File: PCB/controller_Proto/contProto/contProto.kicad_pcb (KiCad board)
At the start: 2 copper layers, 40 parts, among them J1 Conn_01x05, J10 JST_1mm_3, J11 JST_1mm_3, J12 Conn_01x04, J15 Conn_01x04, J16 Conn_01x04, J2 Conn_01x04, J3 Conn_01x05, J4 Conn_01x04, J5 Conn_01x05, J6 Conn_01x05, J7 Conn_01x05, J8 Conn_01x05, J9 Conn_01x04, SW1 SMD_12x12mm_h8.5mm, SW10 SMD_12x12mm_h8.5mm, SW11 SMD_12x12mm_h8.5mm, SW12 SMD_12x12mm_h8.5mm, SW13 SMD_12x12mm_h8.5mm, SW14 SMD_12x12mm_h8.5mm, SW15 SMD_12x12mm_h8.5mm, SW16 SMD_12x12mm_h8.5mm, SW2 SMD_12x12mm_h8.5mm, SW3 SMD_12x12mm_h8.5mm, SW4 SMD_12x12mm_h8.5mm, SW5 SMD_12x12mm_h8.5mm, SW6 SMD_12x12mm_h8.5mm, SW7 SMD_12x12mm_h8.5mm, SW8 SMD_12x12mm_h8.5mm, SW9 SMD_12x12mm_h8.5mm, U1 ProMicroC, U2 ProMicroC, U3 DRV5033FAxLPG, U4 DRV5033FAxLPG

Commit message: pcb fixing
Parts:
- removed J6: Conn_01x05, PCM_SparkFun-Connector:JST_1x05_P1.25mm_Locking_Horizontal_SMD
- removed R1, R2, R3, R4: 1k, PCM_SparkFun-Resistor:R_0402_1005Metric
- removed TP3: TestPoint_2Pole, TestPoint:TestPoint_Bridge_Pitch2.0mm_Drill0.7mm
- added J13: Conn_01x02_Socket, Connector_PinHeader_1.00mm:PinHeader_1x02_P1.00mm_Vertical, F.Cu at (193.9, 66.8)
- added J14: Conn_01x02_Socket, Connector_PinHeader_1.00mm:PinHeader_1x02_P1.00mm_Vertical, F.Cu at (197.3, 66.8)
- added J17: Conn_01x10_Pin, Connector_FFC-FPC:Amphenol_F32Q-1A7x1-11010_1x10-1MP_P0.5mm_Horizontal, F.Cu at (242.1, 69.7)
- added TP1: TestPoint_2Pole, TestPoint:TestPoint_Bridge_Pitch2.0mm_Drill0.7mm, F.Cu at (194.0, 60.1)
- J12, J15, J16, J2, J4, J9: footprint PCM_SparkFun-Connector:JST_1x04_P2.0mm_Horizontal_SMD -> PCM_SparkFun-Connector:JST_1x04_P1.25mm_Locking_Horizontal_SMD
- J3: value Conn_01x05 -> Conn_01x10_Pin; footprint PCM_SparkFun-Connector:JST_1x05_P1.25mm_Locking_Horizontal_SMD -> Connector_FFC-FPC:Amphenol_F32Q-1A7x1-11010_1x10-1MP_P0.5mm_Horizontal
- moved U2 188.1 mm to (235.3, 40.4), turned to 0 degrees
- moved J11 183.9 mm to (238.4, 81.5)
- moved J8 171.7 mm to (197.8, 52.5), turned to 0 degrees
- moved J10 147.2 mm to (238.4, 74.5)
- moved J3 141.0 mm to (242.1, 61.9), turned to 0 degrees
- moved U1 131.5 mm to (213.9, 40.4), turned to 0 degrees
- moved J9 127.8 mm to (185.3, 46.0)
- moved TP4 112.2 mm to (194.0, 63.6)
- moved J2 99.1 mm to (185.3, 24.7)
- moved J5 94.6 mm to (197.8, 34.3), turned to 0 degrees
- moved SW15 77.1 mm to (229.7, 70.6)
- moved U4 76.2 mm to (244.0, 82.0)
- moved J15 58.6 mm to (185.3, 67.3)
- moved SW13 58.5 mm to (229.7, 60.1)
- moved SW14 58.5 mm to (229.7, 65.3)
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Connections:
- J3 pad 1: /Xout -> unconnected-(J3-Pin_1-Pad1)
- J3 pad 2: /Yout -> GND
- J3 pad 3: /Btn -> unconnected-(J3-Pin_3-Pad3)
- J3 pad 4: 3.3V -> GND
- J3 pad 5: GND -> /Btn
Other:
- board text removed: "Dpad"
- board text removed: "Face buttons"
- board text removed: "L"
- board text removed: "Left special"
- board text removed: "R"
- board text removed: "Right special"

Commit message: fixing pcb
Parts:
- removed SW13, SW6: SMD_12x12mm_h8.5mm, Button_Switch_SMD:SW_Tactile_SPST_NO_Straight_CK_PTS636Sx25SMTRLFS
- added J18: JST_1mm_3, Connector_JST:JST_GH_BM03B-GHS-TBT_1x03-1MP_P1.25mm_Vertical, F.Cu at (126.5, 160.8)
- added J19: Conn_01x08_Socket, Connector_PinSocket_1.00mm:PinSocket_1x08_P1.00mm_Vertical, F.Cu at (88.5, 164.5)
- added J20: JST_1mm_3, Connector_JST:JST_GH_BM03B-GHS-TBT_1x03-1MP_P1.25mm_Vertical, F.Cu at (58.0, 126.2)
- added J21: JST_1mm_3, Connector_JST:JST_GH_BM03B-GHS-TBT_1x03-1MP_P1.25mm_Vertical, F.Cu at (116.1, 120.4)
- added J6: JST_1mm_3, Connector_JST:JST_GH_BM03B-GHS-TBT_1x03-1MP_P1.25mm_Vertical, F.Cu at (72.5, 162.2)
- added R1: 1k, PCM_SparkFun-Resistor:R_0402_1005Metric, F.Cu at (80.1, 26.5)
- added R10: 1k, PCM_SparkFun-Resistor:R_0402_1005Metric, F.Cu at (83.0, 32.5)
- added R11: 1k, PCM_SparkFun-Resistor:R_0402_1005Metric, F.Cu at (83.0, 34.5)
- added R12: 1k, PCM_SparkFun-Resistor:R_0402_1005Metric, F.Cu at (83.0, 36.5)
- added R13: 1k, PCM_SparkFun-Resistor:R_0402_1005Metric, F.Cu at (85.9, 26.5)
- added R14: 1k, PCM_SparkFun-Resistor:R_0402_1005Metric, F.Cu at (85.9, 28.5)
- added R15: 1k, PCM_SparkFun-Resistor:R_0402_1005Metric, F.Cu at (85.9, 30.5)
- added R16: 1k, PCM_SparkFun-Resistor:R_0402_1005Metric, F.Cu at (85.9, 32.5)
- added R17: 1k, PCM_SparkFun-Resistor:R_0402_1005Metric, F.Cu at (85.9, 34.5)
- added R18: 1k, PCM_SparkFun-Resistor:R_0402_1005Metric, F.Cu at (85.9, 36.5)
- added R19: 1k, PCM_SparkFun-Resistor:R_0402_1005Metric, F.Cu at (88.8, 26.5)
- added R2: 1k, PCM_SparkFun-Resistor:R_0402_1005Metric, F.Cu at (80.1, 28.5)
- added R20: 1k, PCM_SparkFun-Resistor:R_0402_1005Metric, F.Cu at (88.8, 28.5)
- added R21: 1k, PCM_SparkFun-Resistor:R_0402_1005Metric, F.Cu at (88.8, 30.5)
- added R22: 1k, PCM_SparkFun-Resistor:R_0402_1005Metric, F.Cu at (88.8, 32.5)
- added R3: 1k, PCM_SparkFun-Resistor:R_0402_1005Metric, F.Cu at (80.1, 30.5)
- added R4: 1k, PCM_SparkFun-Resistor:R_0402_1005Metric, F.Cu at (80.1, 32.5)
- added R5: 1k, PCM_SparkFun-Resistor:R_0402_1005Metric, F.Cu at (80.1, 34.5)
- added R6: 1k, PCM_SparkFun-Resistor:R_0402_1005Metric, F.Cu at (80.1, 36.5)
- added R7: 1k, PCM_SparkFun-Resistor:R_0402_1005Metric, F.Cu at (83.0, 26.5)
- added R8: 1k, PCM_SparkFun-Resistor:R_0402_1005Metric, F.Cu at (83.0, 28.5)
- added R9: 1k, PCM_SparkFun-Resistor:R_0402_1005Metric, F.Cu at (83.0, 30.5)
- added SW17: SMD_12x12mm_h8.5mm, Button_Switch_SMD:SW_Tactile_SPST_NO_Straight_CK_PTS636Sx25SMTRLFS, F.Cu at (34.1, 112.8)
- added SW18: SMD_12x12mm_h8.5mm, Button_Switch_SMD:SW_Tactile_SPST_NO_Straight_CK_PTS636Sx25SMTRLFS, F.Cu at (34.1, 118.0)
- J1, J5, J7, J8: footprint PCM_SparkFun-Connector:JST_1x05_P1.25mm_Locking_Horizontal_SMD -> Connector_JST:JST_GH_BM05B-GHS-TBT_1x05-1MP_P1.25mm_Vertical
- J10, J11: footprint PCM_SparkFun-Connector:JST_1x03_P1.0mm_Horizontal_SMD -> Connector_JST:JST_GH_BM03B-GHS-TBT_1x03-1MP_P1.25mm_Vertical
- J12, J4: value Conn_01x04 -> JST_1mm_3; footprint PCM_SparkFun-Connector:JST_1x04_P1.25mm_Locking_Horizontal_SMD -> Connector_JST:JST_GH_BM03B-GHS-TBT_1x03-1MP_P1.25mm_Vertical
- J13, J14: footprint Connector_PinHeader_1.00mm:PinHeader_1x02_P1.00mm_Vertical -> Connector_PinSocket_1.00mm:PinSocket_1x02_P1.00mm_Vertical
- J15, J16, J2, J9: footprint PCM_SparkFun-Connector:JST_1x04_P1.25mm_Locking_Horizontal_SMD -> Connector_JST:JST_GH_BM04B-GHS-TBT_1x04-1MP_P1.25mm_Vertical
- moved J17 215.9 mm to (55.0, 177.5), turned to 90 degrees
- moved J11 195.3 mm to (65.9, 173.1), turned to 180 degrees
- moved U2 191.0 mm to (73.5, 142.0), turned to 90 degrees
- moved J8 176.9 mm to (59.4, 162.7), turned to 90 degrees
- moved J2 172.2 mm to (105.1, 177.1)
- moved J3 164.5 mm to (125.0, 177.5), turned to 90 degrees
- moved J10 153.1 mm to (111.8, 160.4), turned to 180 degrees
- moved U1 143.2 mm to (113.2, 142.1), turned to -90 degrees
- moved J14 138.1 mm to (73.5, 128.0), turned to 90 degrees
- moved J9 132.2 mm to (75.1, 119.0)
- moved TP4 116.7 mm to (94.5, 124.5)
- moved TP1 114.3 mm to (96.0, 119.0), turned to 180 degrees
- moved J5 112.6 mm to (126.1, 121.2), turned to -90 degrees
- moved J13 106.0 mm to (106.0, 126.0), turned to 90 degrees
- moved J1 101.2 mm to (277.0, 88.0)
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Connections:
- J1 pad 1: GND -> /FB_VCC
- J12 pad 1: GND -> /SL_VCC
- J4 pad 1: GND -> /SR_VCC
- J5 pad 1: GND -> VCC
- J7 pad 1: GND -> /D_VCC
- J8 pad 1: GND -> VCC2
- SW1 pad 2: GND -> /FB_VCC
- SW10 pad 2: GND -> /D_VCC
- SW11 pad 2: GND -> /D_VCC
- SW12 pad 2: GND -> /SL_VCC
- SW14 pad 2: GND -> /SL_VCC
- SW15 pad 2: GND_RSP -> VCC_RSP
- SW16 pad 2: GND_LSP -> VCC_LSP
- SW2 pad 2: GND -> /FB_VCC
- SW3 pad 2: GND -> /FB_VCC
- SW4 pad 2: GND -> /FB_VCC
- SW5 pad 2: GND -> /SR_VCC
- SW7 pad 2: GND -> /SR_VCC
- SW8 pad 2: GND -> /D_VCC
- SW9 pad 2: GND -> /D_VCC
- U1 pad 13: unconnected-(U1-D10/A10-Pad13) -> /SP2
- U1 pad 14: unconnected-(U1-D16-Pad14) -> /plus
- U1 pad 15: unconnected-(U1-D14-Pad15) -> /Pad1
- U1 pad 16: unconnected-(U1-D15-Pad16) -> /Pad2
- U1 pad 22: unconnected-(U1-RST-Pad22) -> /RST1
- U2 pad 13: unconnected-(U2-D10/A10-Pad13) -> /minus
- U2 pad 14: unconnected-(U2-D16-Pad14) -> /SP3
- U2 pad 15: unconnected-(U2-D14-Pad15) -> /Pad3
- U2 pad 16: unconnected-(U2-D15-Pad16) -> /Pad4
- U2 pad 22: unconnected-(U2-RST-Pad22) -> /RST2

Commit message: PCB layout
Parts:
- added J22: JST_1mm_3, Connector_JST:JST_GH_BM03B-GHS-TBT_1x03-1MP_P1.25mm_Vertical, B.Cu at (56.4, 150.1)
- added J23: JST_1mm_3, Connector_JST:JST_GH_BM03B-GHS-TBT_1x03-1MP_P1.25mm_Vertical, B.Cu at (43.5, 150.3)
- added SW13: SMD_12x12mm_h8.5mm, Button_Switch_SMD:SW_Tactile_SPST_NO_Straight_CK_PTS636Sx25SMTRLFS, F.Cu at (43.0, 130.2)
- added SW19: SMD_12x12mm_h8.5mm, Button_Switch_SMD:SW_Tactile_SPST_NO_Straight_CK_PTS636Sx25SMTRLFS, F.Cu at (56.6, 130.2)
- added SW20: SMD_12x12mm_h8.5mm, Button_Switch_SMD:SW_Tactile_SPST_NO_Straight_CK_PTS636Sx25SMTRLFS, F.Cu at (56.6, 113.8)
- added SW6: SMD_12x12mm_h8.5mm, Button_Switch_SMD:SW_Tactile_SPST_NO_Straight_CK_PTS636Sx25SMTRLFS, F.Cu at (43.5, 113.8)
- J12, J15, J16, J4, J7: moved to B.Cu
- moved SW8 221.8 mm to (74.1, 144.2)
- moved SW11 210.2 mm to (85.5, 156.9), turned to 90 degrees
- moved SW9 205.8 mm to (85.6, 135.8), turned to 90 degrees
- moved J7 195.3 mm to (98.7, 125.9), turned to 180 degrees
- moved SW10 194.9 mm to (98.9, 144.2)
- moved SW7 189.8 mm to (57.9, 103.5), turned to 180 degrees
- moved SW12 188.5 mm to (29.1, 113.2)
- moved J12 187.2 mm to (29.6, 95.9), turned to 180 degrees
- moved U4 185.5 mm to (83.8, 111.2), turned to -90 degrees
- moved SW15 181.3 mm to (97.0, 112.4), turned to 90 degrees
- moved SW5 180.3 mm to (71.4, 113.2)
- moved J4 174.4 mm to (73.1, 96.4), turned to 180 degrees
- moved SW14 173.3 mm to (42.6, 103.5)
- moved J16 159.8 mm to (110.1, 113.0), turned to 90 degrees
- moved J2 155.5 mm to (87.1, 22.6)
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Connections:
- R12 pad 1: unconnected-(R12-Pad1) -> /Btn
- R18 pad 1: unconnected-(R18-Pad1) -> /Btn2
- SW7 pad 1: /Btn_SP -> /Btn_SP2
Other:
- board outline added: 91.8 x 145.2 mm

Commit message: pcbeing
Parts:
- J17, J3, J5, J8: moved to B.Cu
- moved J17 77.4 mm to (105.2, 65.5)
- moved J3 76.7 mm to (28.1, 82.0)
- moved J5 76.3 mm to (28.3, 65.2)
- moved J8 75.8 mm to (104.3, 82.5)
- moved SW9 3.75 mm to (85.6, 132.0)
- turned J7 to 0 degrees
- turned SW11 to -90 degrees
- turned SW5 to 180 degrees
- turned SW8 to 180 degrees
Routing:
- net /SR_VCC: vias 0 -> 1
- net /SL_VCC: vias 0 -> 1
- net /D_VCC: vias 0 -> 1
- net /Btn_U: vias 0 -> 1
- net /Btn_SP3: vias 0 -> 1
- net /Btn_SP2: vias 0 -> 1
- net /Btn_R: vias 0 -> 1
- net /Btn_L: vias 0 -> 1
- net /Btn_D: vias 0 -> 1
- net /Btn_-: vias 0 -> 1
- net /Btn_+: vias 0 -> 1
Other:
- board size 91.8 x 145.2 mm -> 95 x 146.5 mm

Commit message: ALL THE PLANES
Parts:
- J17, J3, J5, J8: moved to F.Cu
- R1, R10, R11, R12, R13, R14, R15, R16, R17, R18, R19, R2, R20, R21, R22, R3, R4, R5, R6, R7, R8, R9: moved to B.Cu
- moved J8 79.8 mm to (24.5, 82.5), turned to -90 degrees
- moved J17 78.9 mm to (26.2, 66.2)
- moved J5 77.7 mm to (106.0, 65.5)
- moved J3 77.2 mm to (105.3, 81.2)
- moved R12 45.7 mm to (77.0, 41.5)
- moved R11 37.9 mm to (55.0, 40.8), turned to 180 degrees
- moved R17 37.2 mm to (57.5, 40.8), turned to 180 degrees
- moved R21 36.7 mm to (57.7, 51.8)
- moved R16 36.1 mm to (55.0, 51.8)
- moved R6 36.0 mm to (48.0, 50.5), turned to 90 degrees
- moved R7 35.9 mm to (52.7, 51.8)
- moved R1 34.5 mm to (73.0, 41.5), turned to 0 degrees
- moved R13 32.0 mm to (39.7, 35.0)
- moved R20 30.8 mm to (73.0, 51.2), turned to 0 degrees
- moved R15 30.5 mm to (77.5, 50.7)
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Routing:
- net SDA: track 0.00 -> 82.4 mm, vias 0 -> 2
- net /Btn: track 0.00 -> 73.7 mm, vias 0 -> 2
- net SCL: track 0.00 -> 68.9 mm, vias 0 -> 2
- net /A32: track 0.00 -> 60.9 mm, vias 0 -> 2
- net GND: track 0.00 -> 57.4 mm, vias 0 -> 26
- net /D: track 0.00 -> 56.1 mm, vias 0 -> 2
- net /R: track 0.00 -> 52.9 mm, vias 0 -> 2
- net /R2: track 0.00 -> 50.8 mm, vias 0 -> 2
- net /Pad4: track 0.00 -> 48.9 mm, vias 0 -> 3
- net /X: track 0.00 -> 48.6 mm, vias 0 -> 3
- net /X2out: track 0.00 -> 47.1 mm, vias 0 -> 1
- net /Pad3: track 0.00 -> 47.0 mm, vias 0 -> 3
- net /L: track 0.00 -> 46.8 mm, vias 0 -> 2
- net /Y2out: track 0.00 -> 46.6 mm, vias 0 -> 1
- net /U: track 0.00 -> 46.0 mm, vias 0 -> 3
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- added copper zone on B.Cu, net /D_VCC
- added copper zone on B.Cu, net /SL_VCC
- added copper zone on B.Cu, net /SR_VCC
- added copper zone on F.Cu, net GND
- added copper zone on B.Cu, net VCC
- added copper zone on B.Cu, net VCC2
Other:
- board size 95 x 146.5 mm -> 92.2 x 146.2 mm
- copper layers 2 -> 4

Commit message: face but
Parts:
- J1: moved to B.Cu
- moved SW2 112.2 mm to (121.0, 35.0), turned to 180 degrees
- moved J1 108.8 mm to (119.0, 49.5), turned to -90 degrees
- moved SW1 103.9 mm to (133.0, 23.0), turned to 90 degrees
- moved SW4 100.5 mm to (133.0, 47.0), turned to -90 degrees
- moved SW3 92.4 mm to (145.1, 35.0)
- moved SW10 80.3 mm to (144.2, 80.6)
- moved J7 80.3 mm to (144.6, 62.2)
- moved SW11 80.3 mm to (131.5, 92.6)
- moved SW8 80.3 mm to (120.1, 80.6)
- moved SW9 80.3 mm to (131.6, 68.3)
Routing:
- net /Btn_B: track 0.00 -> 26.8 mm, vias 0 -> 1
- net /Btn_Y: track 0.00 -> 26.3 mm, vias 0 -> 1
- net /Btn_X: track 0.00 -> 18.6 mm, vias 0 -> 1
- net /Btn_A: track 0.00 -> 15.7 mm, vias 0 -> 1
- net /FB_VCC: vias 0 -> 4
- added copper zone on B.Cu, net /FB_VCC
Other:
- board size 92.2 x 146.2 mm -> 132.2 x 138 mm

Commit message: finnish shoulder borads
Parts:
- added J24: Conn_01x03_Socket, Connector_PinSocket_2.54mm:PinSocket_1x03_P2.54mm_Vertical, F.Cu at (87.4, 121.6)
- added J25: Conn_01x03_Socket, Connector_PinSocket_2.54mm:PinSocket_1x03_P2.54mm_Vertical, F.Cu at (66.3, 125.4)
- added J26: Conn_01x03_Socket, Connector_PinSocket_2.54mm:PinSocket_1x03_P2.54mm_Vertical, F.Cu at (95.5, 136.5)
- added J27: Conn_01x03_Socket, Connector_PinSocket_2.54mm:PinSocket_1x03_P2.54mm_Vertical, F.Cu at (101.1, 121.6)
- added J28: Conn_01x12_Socket, Connector_PinSocket_2.54mm:PinSocket_1x12_P2.54mm_Vertical, F.Cu at (100.4, 37.5)
- added J29: Conn_01x12_Socket, Connector_PinSocket_2.54mm:PinSocket_1x12_P2.54mm_Vertical, F.Cu at (72.5, 55.0)
- added J30: Conn_01x12_Socket, Connector_PinSocket_2.54mm:PinSocket_1x12_P2.54mm_Vertical, F.Cu at (35.2, 55.0)
- added J31: Conn_01x12_Socket, Connector_PinSocket_2.54mm:PinSocket_1x12_P2.54mm_Vertical, F.Cu at (35.2, 37.0)
- J19: footprint Connector_PinSocket_1.00mm:PinSocket_1x08_P1.00mm_Vertical -> Connector_PinSocket_2.54mm:PinSocket_1x08_P2.54mm_Vertical
- moved U3 39.2 mm to (84.5, 135.5), turned to 90 degrees
- moved U4 28.4 mm to (67.7, 136.4), turned to 0 degrees
- moved J16 22.6 mm to (89.7, 98.0), turned to 180 degrees
- moved SW16 14.7 mm to (103.6, 109.6), turned to 180 degrees
- moved SW15 4.73 mm to (89.5, 110.1), turned to 180 degrees
- moved J19 3.91 mm to (60.1, 65.5)
- moved J15 2.48 mm to (104.0, 97.8), turned to 180 degrees
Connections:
- U3 pad 1: VCC_LSP -> VCC_LSP2
- U3 pad 2: GND_LSP -> GND_LSP2
- U3 pad 3: /L2P -> /L2P2
- U4 pad 1: VCC_RSP -> VCC_RSP2
- U4 pad 2: GND_RSP -> GND_RSP2
- U4 pad 3: /R2P -> /R2P2
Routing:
- net /X: track 48.6 -> 74.1 mm, vias 3 -> 2
- net /R2P: track 0.00 -> 22.6 mm, vias 0 -> 1
- net /L2P: track 0.00 -> 22.5 mm, vias 0 -> 1
- net GND_LSP: track 0.00 -> 22.3 mm, vias 0 -> 1
- net GND_RSP: track 0.00 -> 21.9 mm, vias 0 -> 1
- net /Btn: track 73.7 -> 60.0 mm, vias 2 -> 1
- net /L2P2: track 0.00 -> 11.6 mm
- net VCC_RSP2: track 0.00 -> 11.6 mm
- net /R2P2: track 0.00 -> 11.4 mm
- net VCC_LSP2: track 0.00 -> 11.4 mm
- net GND_LSP2: track 0.00 -> 11.1 mm
- net GND_RSP2: track 0.00 -> 11.1 mm
- net /R1P: track 0.00 -> 10.9 mm, vias 0 -> 1
- net /L1P: track 0.00 -> 10.6 mm, vias 0 -> 1
- net SDA: track 82.4 -> 72.9 mm, vias 2 -> 0
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- added copper zone on B.Cu, net VCC_LSP
- added copper zone on B.Cu, net VCC_RSP
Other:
- outline, holes or cut-outs redrawn

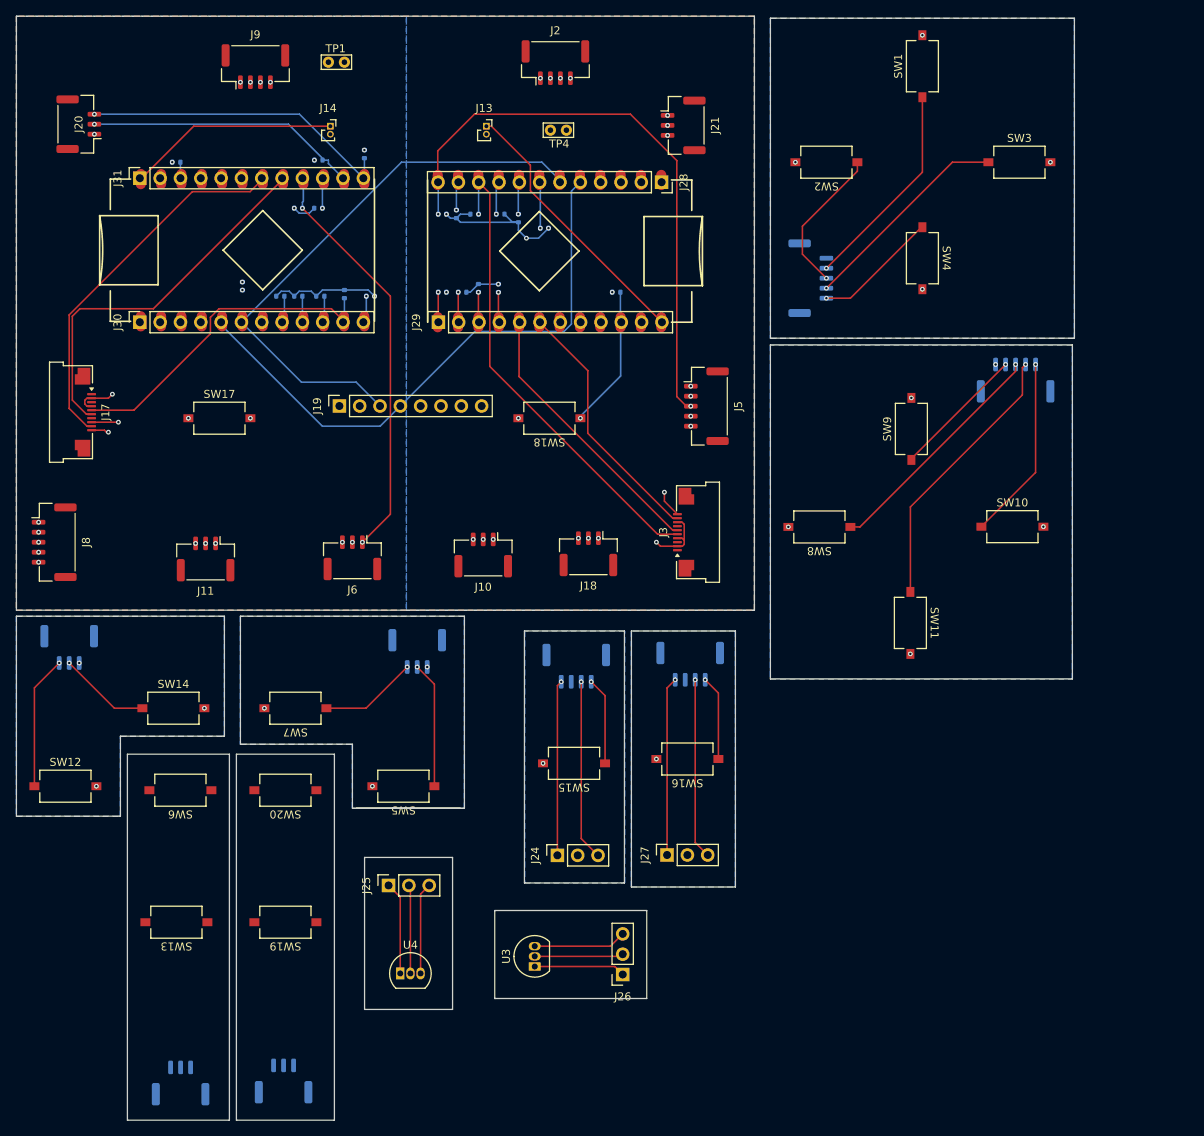
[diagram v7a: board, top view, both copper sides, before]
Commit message: failing with mouse bites
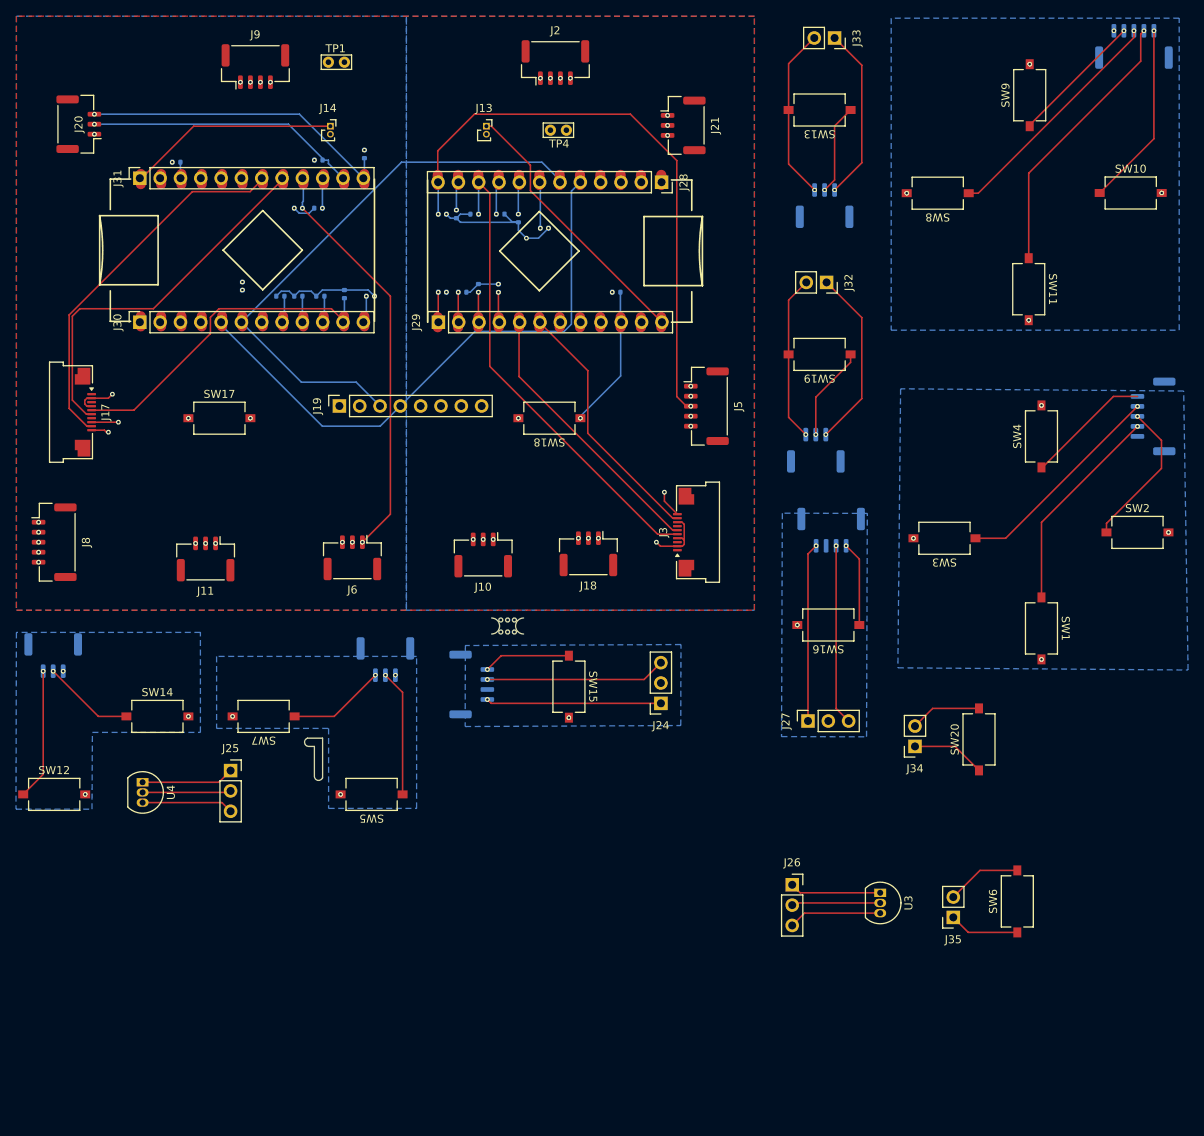
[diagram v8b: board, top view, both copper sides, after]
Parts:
- added J32: Conn_01x02_Socket, Connector_PinSocket_2.54mm:PinSocket_1x02_P2.54mm_Vertical, F.Cu at (121.0, 50.0)
- added J33: Conn_01x02_Socket, Connector_PinSocket_2.54mm:PinSocket_1x02_P2.54mm_Vertical, F.Cu at (122.0, 19.5)
- added J34: Conn_01x02_Socket, Connector_PinSocket_2.54mm:PinSocket_1x02_P2.54mm_Vertical, F.Cu at (132.1, 108.0)
- added J35: Conn_01x02_Socket, Connector_PinSocket_2.54mm:PinSocket_1x02_P2.54mm_Vertical, F.Cu at (136.9, 129.4)
- added REF**: MouseBite-Slot_2.0x2.0mm_outset_D0.5mm_P0.85mm_3h, Panelization:MouseBite-Slot_2.0x2.0mm_outset_D0.5mm_P0.85mm_3h, F.Cu at (81.2, 94.0)
- moved J23 136.0 mm to (120.8, 40.4)
- moved SW13 129.5 mm to (120.2, 28.5)
- moved SW6 105.5 mm to (144.9, 127.4), turned to 90 degrees
- moved J22 103.2 mm to (119.7, 71.0)
- moved SW19 97.4 mm to (120.2, 59.0)
- moved SW20 86.9 mm to (140.1, 107.2), turned to 90 degrees
- moved SW1 71.8 mm to (147.9, 93.3), turned to -90 degrees
- moved SW2 60.4 mm to (159.9, 81.3), turned to 0 degrees
- moved SW3 47.9 mm to (135.8, 82.0), turned to 180 degrees
- moved J1 46.1 mm to (161.8, 66.8), turned to 90 degrees
- moved SW11 44.3 mm to (146.3, 50.9)
- moved SW8 44.3 mm to (134.9, 38.9)
- moved SW9 44.3 mm to (146.4, 26.6)
- moved J7 44.3 mm to (159.4, 20.5)
- moved SW10 44.3 mm to (159.0, 38.8)
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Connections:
- SW20 pad 1: /PP4 -> /PP42
- SW20 pad 2: /PPVCC2 -> /PPVCC22
- SW6 pad 1: /PP2 -> /PP22
- SW6 pad 2: /PPVCC1 -> /PPVCC12
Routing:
- net /PP4: track 0.00 -> 22.7 mm, vias 0 -> 1
- net /PP2: track 0.00 -> 21.8 mm, vias 0 -> 1
- net /PPVCC1: track 0.00 -> 21.7 mm, vias 0 -> 1
- net /PPVCC2: track 0.00 -> 20.8 mm, vias 0 -> 1
- net /PP3: track 0.00 -> 11.8 mm, vias 0 -> 1
- net /PP1: track 0.00 -> 11.3 mm, vias 0 -> 1
- net /PPVCC12: track 0.00 -> 9.38 mm
- net /PP42: track 0.00 -> 9.24 mm
- net /PPVCC22: track 0.00 -> 8.92 mm
- net /PP22: track 0.00 -> 8.78 mm
- net /Btn_A: vias 1 -> 0
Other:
- board size 132.2 x 138 mm -> 2.3 x 5.3 mm
